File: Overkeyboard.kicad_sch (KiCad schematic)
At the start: 329 parts, among them SW1 SW_Push, SW10 SW_Push, SW100 SW_Push, SW101 SW_Push, SW102 SW_Push, SW103 SW_Push, SW104 SW_Push, SW105 SW_Push, SW106 SW_Push, SW107 SW_Push, SW108 SW_Push, SW109 SW_Push, SW11 SW_Push, SW110 SW_Push, SW111 SW_Push, SW112 SW_Push, SW113 SW_Push, SW114 SW_Push, SW115 SW_Push, SW116 SW_Push, SW117 SW_Push, SW118 SW_Push, SW119 SW_Push, SW12 SW_Push, SW120 SW_Push, SW121 SW_Push, SW122 SW_Push, SW123 SW_Push, SW124 SW_Push, SW125 SW_Push, SW126 SW_Push, SW127 SW_Push, SW128 SW_Push, SW129 SW_Push, SW13 SW_Push, SW130 SW_Push, SW131 SW_Push, SW132 SW_Push, SW133 SW_Push, SW134 SW_Push, SW135 SW_Push, SW136 SW_Push, SW137 SW_Push, SW138 SW_Push, SW139 SW_Push, SW14 SW_Push, SW140 SW_Push, SW141 SW_Push, SW142 SW_Push, SW143 SW_Push, SW144 SW_Push, SW145 SW_Push, SW146 SW_Push, SW147 SW_Push, SW148 SW_Push, SW149 SW_Push, SW15 SW_Push, SW150 SW_Push, SW151 SW_Push, SW152 SW_Push, SW153 SW_Push, SW154 SW_Push, SW155 SW_Push, SW156 SW_Push, SW157 SW_Push, SW16 SW_Push, SW17 SW_Push, SW18 SW_Push, SW19 SW_Push, SW2 SW_Push, SW20 SW_Push, SW21 SW_Push, SW22 SW_Push, SW23 SW_Push, SW24 SW_Push, SW25 SW_Push, SW26 SW_Push, SW27 SW_Push, SW28 SW_Push, SW29 SW_Push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

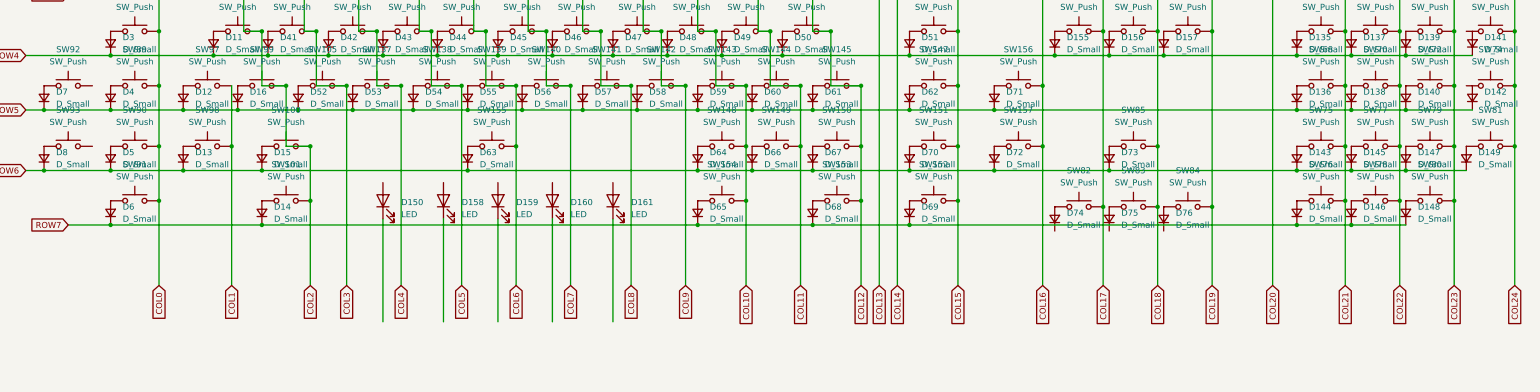
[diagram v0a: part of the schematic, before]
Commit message: added footprints
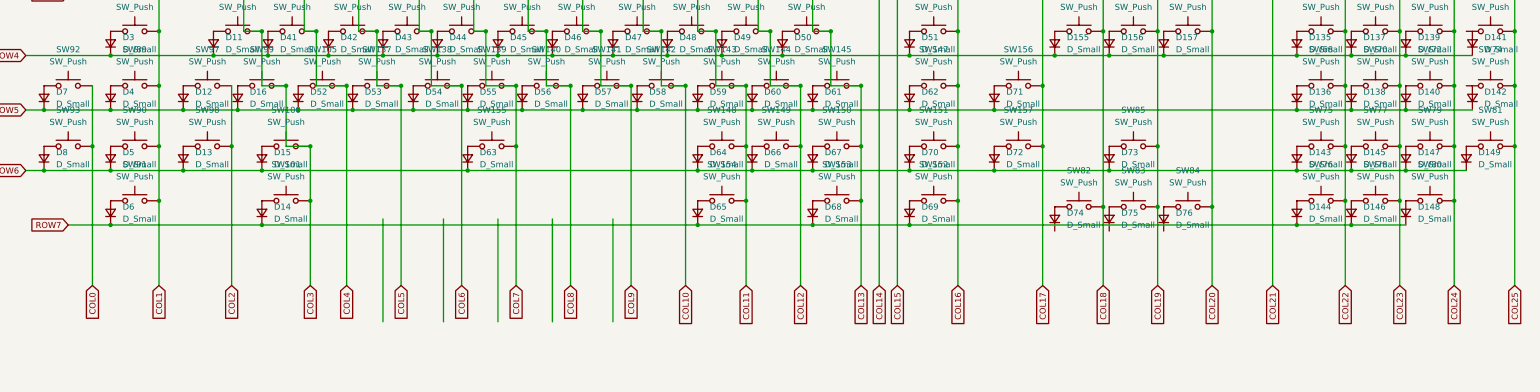
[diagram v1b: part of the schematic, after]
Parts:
- removed D150, D158, D159, D160, D161: LED, symbol Device:LED
- C1, C2, C3: footprint (none) -> Capacitor_SMD:C_0805_2012Metric_Pad1.18x1.45mm_HandSolder
- D1, D10, D100, D101, D102, D103, D104, D105, D106, D107, D108, D109, D11, D110, D111, D112, D113, D114, D115, D116, D117, D118, D119, D12, D120, D121, D122, D123, D124, D125, D126, D127, D128, D129, D13, D130, D131, D132, D133, D134, D135, D136, D137, D138, D139, D14, D140, D141, D142, D143, D144, D145, D146, D147, D148, D149, D15, D151, D152, D153, D154, D155, D156, D157, D16, D17, D18, D19, D2, D20, D21, D22, D23, D24, D25, D26, D27, D28, D29, D3, D30, D31, D32, D33, D34, D35, D36, D37, D38, D39, D4, D40, D41, D42, D43, D44, D45, D46, D47, D48, D49, D5, D50, D51, D52, D53, D54, D55, D56, D57, D58, D59, D6, D60, D61, D62, D63, D64, D65, D66, D67, D68, D69, D7, D70, D71, D72, D73, D74, D75, D76, D77, D78, D79, D8, D80, D81, D82, D83, D84, D85, D86, D87, D88, D89, D9, D90, D91, D92, D93, D94, D95, D96, D97, D98, D99: footprint (none) -> Diode_SMD:D_SOD-123
- F1: footprint (none) -> Fuse:Fuse_1206_3216Metric_Pad1.42x1.75mm_HandSolder
- R1, R2, R3, R4: footprint (none) -> Resistor_SMD:R_0805_2012Metric_Pad1.20x1.40mm_HandSolder
- SW1: footprint (none) -> random-keyboard-parts:SKQG-1155865
- SW10, SW100, SW101, SW102, SW103, SW104, SW105, SW106, SW107, SW108, SW109, SW11, SW110, SW111, SW112, SW113, SW114, SW115, SW116, SW117, SW118, SW119, SW12, SW120, SW121, SW122, SW123, SW124, SW125, SW126, SW127, SW128, SW129, SW13, SW130, SW131, SW132, SW133, SW134, SW135, SW136, SW137, SW138, SW139, SW14, SW140, SW141, SW142, SW143, SW144, SW145, SW146, SW147, SW148, SW149, SW15, SW150, SW151, SW152, SW153, SW154, SW155, SW156, SW157, SW16, SW17, SW18, SW19, SW2, SW20, SW21, SW22, SW23, SW24, SW25, SW26, SW27, SW28, SW29, SW3, SW30, SW31, SW32, SW33, SW34, SW35, SW36, SW37, SW38, SW39, SW4, SW40, SW41, SW42, SW43, SW44, SW45, SW46, SW47, SW48, SW49, SW5, SW50, SW51, SW52, SW53, SW54, SW55, SW56, SW57, SW58, SW59, SW6, SW60, SW61, SW62, SW63, SW64, SW65, SW66, SW67, SW68, SW69, SW7, SW70, SW71, SW72, SW73, SW74, SW75, SW76, SW77, SW78, SW79, SW8, SW80, SW81, SW82, SW83, SW84, SW85, SW86, SW87, SW88, SW89, SW9, SW90, SW91, SW92, SW93, SW94, SW95, SW96, SW97, SW98, SW99: footprint (none) -> MX_Alps_Hybrid:MX-Alps-Hybrid-1U
- USB1: footprint (none) -> random-keyboard-parts:Molex-0548190589
- Y1: footprint (none) -> Crystal:Crystal_SMD_3225-4Pin_3.2x2.5mm_HandSoldering
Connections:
- net COL0: now also SW92.2, SW93.2; no longer SW2.2, SW3.2, SW86.2, SW87.2, SW88.2, SW89.2, SW90.2, SW91.2
- net COL1: now also SW2.2, SW3.2, SW86.2, SW87.2, SW88.2, SW89.2, SW90.2, SW91.2; no longer SW97.2, SW98.2
- net COL10: now also SW111.2, SW123.2, SW133.2, SW142.2, SW16.2, SW17.2; no longer SW112.2, SW124.2, SW134.2, SW143.2, SW148.2, SW154.2, SW18.2, SW19.2
- net COL11: now also SW112.2, SW124.2, SW134.2, SW143.2, SW148.2, SW154.2, SW18.2, SW19.2; no longer SW113.2, SW125.2, SW135.2, SW144.2, SW149.2
- net COL12: now also SW113.2, SW125.2, SW135.2, SW144.2, SW149.2; no longer SW114.2, SW126.2, SW136.2, SW145.2, SW150.2, SW153.2, SW20.2, SW21.2
- net COL13: now also SW114.2, SW126.2, SW136.2, SW145.2, SW150.2, SW153.2, SW20.2, SW21.2; no longer SW115.2, SW127.2, SW22.2, SW23.2
- net COL14: now also SW115.2, SW127.2, SW22.2, SW23.2; no longer SW116.2, SW24.2, SW25.2
- net COL15: now also SW116.2, SW24.2, SW25.2; no longer SW117.2, SW146.2, SW147.2, SW151.2, SW152.2, SW26.2, SW27.2
- net COL16: now also SW117.2, SW146.2, SW147.2, SW151.2, SW152.2, SW26.2, SW27.2; no longer SW156.2, SW157.2, SW28.2, SW29.2, SW46.2, SW47.2
- net COL17: now also SW156.2, SW157.2, SW28.2, SW29.2, SW46.2, SW47.2; no longer SW30.2, SW31.2, SW48.2, SW49.2, SW56.2, SW82.2
- net COL18: now also SW30.2, SW31.2, SW48.2, SW49.2, SW56.2, SW82.2; no longer SW32.2, SW33.2, SW50.2, SW51.2, SW57.2, SW83.2, SW85.2
- net COL19: now also SW32.2, SW33.2, SW50.2, SW51.2, SW57.2, SW83.2, SW85.2; no longer SW34.2, SW35.2, SW52.2, SW53.2, SW58.2, SW84.2
- net COL2: now also SW97.2, SW98.2; no longer SW100.2, SW101.2, SW94.2, SW95.2, SW96.2, SW99.2
- net COL20: now also SW34.2, SW35.2, SW52.2, SW53.2, SW58.2, SW84.2; no longer SW36.2, SW37.2, SW54.2, SW55.2
- net COL21: now also SW36.2, SW37.2, SW54.2, SW55.2; no longer SW38.2, SW39.2, SW59.2, SW60.2, SW67.2, SW68.2, SW75.2, SW76.2
- net COL22: now also SW38.2, SW39.2, SW59.2, SW60.2, SW67.2, SW68.2, SW75.2, SW76.2; no longer SW40.2, SW41.2, SW61.2, SW62.2, SW69.2, SW70.2, SW77.2, SW78.2
- net COL23: now also SW40.2, SW41.2, SW61.2, SW62.2, SW69.2, SW70.2, SW77.2, SW78.2; no longer SW42.2, SW43.2, SW63.2, SW64.2, SW71.2, SW72.2, SW79.2, SW80.2
- net COL24: now also SW42.2, SW43.2, SW63.2, SW64.2, SW71.2, SW72.2, SW79.2, SW80.2; no longer SW44.2, SW45.2, SW65.2, SW66.2, SW73.2, SW74.2, SW81.2
- net COL3: now also SW100.2, SW101.2, SW94.2, SW95.2, SW96.2, SW99.2; no longer SW102.2, SW103.2, SW104.2, SW105.2, SW4.2, SW5.2
- net COL4: now also SW102.2, SW103.2, SW104.2, SW105.2, SW4.2, SW5.2; no longer SW106.2, SW118.2, SW128.2, SW137.2, SW6.2, SW7.2
- net COL5: now also SW106.2, SW118.2, SW128.2, SW137.2, SW6.2, SW7.2; no longer SW107.2, SW119.2, SW129.2, SW138.2, SW8.2, SW9.2
- net COL6: now also SW107.2, SW119.2, SW129.2, SW138.2, SW8.2, SW9.2; no longer SW10.2, SW108.2, SW11.2, SW120.2, SW130.2, SW139.2, SW155.2
- net COL7: now also SW10.2, SW108.2, SW11.2, SW120.2, SW130.2, SW139.2, SW155.2; no longer SW109.2, SW12.2, SW121.2, SW13.2, SW131.2, SW140.2
- net COL8: now also SW109.2, SW12.2, SW121.2, SW13.2, SW131.2, SW140.2; no longer SW110.2, SW122.2, SW132.2, SW14.2, SW141.2, SW15.2
- net COL9: now also SW110.2, SW122.2, SW132.2, SW14.2, SW141.2, SW15.2; no longer SW111.2, SW123.2, SW133.2, SW142.2, SW16.2, SW17.2
- new net COL25: SW44.2, SW45.2, SW65.2, SW66.2, SW73.2, SW74.2, SW81.2

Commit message: It should be fully wired now
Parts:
- added C4, C5, C6: 0.1μF, Capacitor_SMD:C_0805_2012Metric_Pad1.18x1.45mm_HandSolder, symbol Device:C_Small
- added C7: 10μF, Capacitor_SMD:C_0805_2012Metric_Pad1.18x1.45mm_HandSolder, symbol Device:C_Small
- SW100, SW148, SW149, SW150, SW151, SW154, SW156, SW157, SW89, SW90, SW92, SW93, SW98: footprint MX_Alps_Hybrid:MX-Alps-Hybrid-1U -> MX_Alps_Hybrid:MX-Alps-Hybrid-1.25U
- SW101, SW147, SW152, SW88: footprint MX_Alps_Hybrid:MX-Alps-Hybrid-1U -> MX_Alps_Hybrid:MX-Alps-Hybrid-1.75U
- SW146: footprint MX_Alps_Hybrid:MX-Alps-Hybrid-1U -> MX_Alps_Hybrid:MX-Alps-Hybrid-ISO
- SW153, SW91: footprint MX_Alps_Hybrid:MX-Alps-Hybrid-1U -> MX_Alps_Hybrid:MX-Alps-Hybrid-2U
- SW155: footprint MX_Alps_Hybrid:MX-Alps-Hybrid-1U -> MX_Alps_Hybrid:MX-Alps-Hybrid-6.25U
- SW81: footprint MX_Alps_Hybrid:MX-Alps-Hybrid-1U -> MX_Alps_Hybrid:MX-Alps-Hybrid-2U-Vertical
- SW87: footprint MX_Alps_Hybrid:MX-Alps-Hybrid-1U -> MX_Alps_Hybrid:MX-Alps-Hybrid-1.5U
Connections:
- net +5V: now also C4.1, C5.1, C6.1, C7.1
- net COL0: now also SW92.1, SW93.1, U1.33 (PE0); no longer SW92.2, SW93.2
- net COL1: now also SW2.1, SW3.1, SW86.1, SW87.1, SW88.1, SW89.1, SW90.1, SW91.1, U1.34 (PE1); no longer SW2.2, SW3.2, SW86.2, SW87.2, SW88.2, SW89.2, SW90.2, SW91.2
- net COL10: now also SW111.1, SW123.1, SW133.1, SW142.1, SW16.1, SW17.1, U1.44 (PA7); no longer SW111.2, SW123.2, SW133.2, SW142.2, SW16.2, SW17.2
- net COL11: now also SW112.1, SW124.1, SW134.1, SW143.1, SW148.1, SW154.1, SW18.1, SW19.1, U1.45 (PA6); no longer SW112.2, SW124.2, SW134.2, SW143.2, SW148.2, SW154.2, SW18.2, SW19.2
- net COL12: now also SW113.1, SW125.1, SW135.1, SW144.1, SW149.1, SW153.1, U1.46 (PA5); no longer SW113.2, SW125.2, SW135.2, SW144.2, SW149.2
- net COL13: now also SW114.1, SW126.1, SW136.1, SW145.1, SW150.1, SW20.1, SW21.1, U1.47 (PA4); no longer SW114.2, SW126.2, SW136.2, SW145.2, SW150.2, SW153.2, SW20.2, SW21.2
- net COL14: now also SW115.1, SW127.1, SW22.1, SW23.1, U1.48 (PA3); no longer SW115.2, SW127.2, SW22.2, SW23.2
- net COL15: now also SW116.1, SW24.1, SW25.1, U1.49 (PA2); no longer SW116.2, SW24.2, SW25.2
- net COL16: now also SW117.1, SW146.1, SW147.1, SW151.1, SW152.1, SW26.1, SW27.1, U1.50 (PA1); no longer SW117.2, SW146.2, SW147.2, SW151.2, SW152.2, SW26.2, SW27.2
- net COL17: now also SW156.1, SW157.1, SW28.1, SW29.1, SW46.1, SW47.1, U1.51 (PA0); no longer SW156.2, SW157.2, SW28.2, SW29.2, SW46.2, SW47.2
- net COL18: now also SW30.1, SW31.1, SW48.1, SW49.1, SW56.1, SW82.1, U1.61 (PF0); no longer SW30.2, SW31.2, SW48.2, SW49.2, SW56.2, SW82.2
- net COL19: now also SW32.1, SW33.1, SW50.1, SW51.1, SW57.1, SW83.1, SW85.1, U1.60 (PF1); no longer SW32.2, SW33.2, SW50.2, SW51.2, SW57.2, SW83.2, SW85.2
- net COL2: now also SW97.1, SW98.1, U1.35 (PC0); no longer SW97.2, SW98.2
- net COL20: now also SW34.1, SW35.1, SW52.1, SW53.1, SW58.1, SW84.1, U1.59 (PF2); no longer SW34.2, SW35.2, SW52.2, SW53.2, SW58.2, SW84.2
- net COL21: now also SW36.1, SW37.1, SW54.1, SW55.1, U1.58 (PF3); no longer SW36.2, SW37.2, SW54.2, SW55.2
- net COL22: now also SW38.1, SW39.1, SW59.1, SW60.1, SW67.1, SW68.1, SW75.1, SW76.1, U1.57 (PF4); no longer SW38.2, SW39.2, SW59.2, SW60.2, SW67.2, SW68.2, SW75.2, SW76.2
- net COL23: now also SW40.1, SW41.1, SW61.1, SW62.1, SW69.1, SW70.1, SW77.1, SW78.1, U1.56 (PF5); no longer SW40.2, SW41.2, SW61.2, SW62.2, SW69.2, SW70.2, SW77.2, SW78.2
- net COL24: now also SW42.1, SW43.1, SW63.1, SW64.1, SW71.1, SW72.1, SW79.1, SW80.1, U1.55 (PF6); no longer SW42.2, SW43.2, SW63.2, SW64.2, SW71.2, SW72.2, SW79.2, SW80.2
- net COL25: now also SW44.1, SW45.1, SW65.1, SW66.1, SW73.1, SW74.1, SW81.1, U1.54 (PF7); no longer SW44.2, SW45.2, SW65.2, SW66.2, SW73.2, SW74.2, SW81.2
- net COL3: now also SW100.1, SW101.1, SW94.1, SW95.1, SW96.1, SW99.1, U1.36 (PC1); no longer SW100.2, SW101.2, SW94.2, SW95.2, SW96.2, SW99.2
- net COL4: now also SW102.1, SW103.1, SW104.1, SW105.1, SW4.1, SW5.1, U1.37 (PC2); no longer SW102.2, SW103.2, SW104.2, SW105.2, SW4.2, SW5.2
- net COL5: now also SW106.1, SW118.1, SW128.1, SW137.1, SW6.1, SW7.1, U1.38 (PC3); no longer SW106.2, SW118.2, SW128.2, SW137.2, SW6.2, SW7.2
- net COL6: now also SW107.1, SW119.1, SW129.1, SW138.1, SW8.1, SW9.1, U1.39 (PC4); no longer SW107.2, SW119.2, SW129.2, SW138.2, SW8.2, SW9.2
- net COL7: now also SW10.1, SW108.1, SW11.1, SW120.1, SW130.1, SW139.1, SW155.1, U1.40 (PC5); no longer SW10.2, SW108.2, SW11.2, SW120.2, SW130.2, SW139.2, SW155.2
- net COL8: now also SW109.1, SW12.1, SW121.1, SW13.1, SW131.1, SW140.1, U1.41 (PC6); no longer SW109.2, SW12.2, SW121.2, SW13.2, SW131.2, SW140.2
- net COL9: now also SW110.1, SW122.1, SW132.1, SW14.1, SW141.1, SW15.1, U1.42 (PC7); no longer SW110.2, SW122.2, SW132.2, SW14.2, SW141.2, SW15.2
- net GND: now also C4.2, C5.2, C6.2, C7.2
- net ROW0: now also D101.1 (K), D103.1 (K), D105.1 (K), D107.1 (K), D109.1 (K), D119.1 (K), D121.1 (K), D123.1 (K), D125.1 (K), D151.1 (K), U1.9 (PE3)
- net ROW1: now also U1.10 (PB0)
- net ROW2: now also U1.11 (PB1)
- net ROW3: now also U1.12 (PB2)
- net ROW4: now also D7.1 (K), U1.13 (PB3)
- net ROW5: now also D8.1 (K), U1.14 (PB4); no longer D7.1 (K)
- net ROW6: now also U1.15 (PB5); no longer D8.1 (K)
- net ROW7: now also D74.1 (K), D75.1 (K), D76.1 (K), U1.16 (PB6)
- net VCC: now also USB1.5 (VBUS); no longer USB1.6 (SHIELD)
- net at D20.2 (A): now also SW107.2; no longer SW107.1
- net at D21.2 (A): now also SW108.2; no longer SW108.1
- net at D62.2 (A): now also SW147.2; no longer SW147.1
- net at D13.2 (A): now also SW98.2; no longer SW98.1
- net at D103.2 (A): now also SW28.2; no longer SW28.1
- net at D30.2 (A): now also SW117.2; no longer SW117.1
- net at D54.2 (A): now also SW138.2; no longer SW138.1
- net at D64.2 (A): now also SW148.2; no longer SW148.1
- net at D122.2 (A): now also SW41.2; no longer SW41.1
- net at D126.2 (A): now also SW45.2; no longer SW45.1
- net at D87.2 (A): now also SW12.2; no longer SW12.1
- net at D73.2 (A): now also SW85.2; no longer SW85.1
- net at D46.2 (A): now also SW132.2; no longer SW132.1
- net at D67.2 (A): now also SW150.2; no longer SW150.1
- net at D34.2 (A): now also SW121.2; no longer SW121.1
- net at D138.2 (A): now also SW70.2; no longer SW70.1
- net at D4.2 (A): now also SW89.2; no longer SW89.1
- net at D127.2 (A): now also SW59.2; no longer SW59.1
- net at D109.2 (A): now also SW34.2; no longer SW34.1
- net at D55.2 (A): now also SW139.2; no longer SW139.1
- net at D56.2 (A): now also SW140.2; no longer SW140.1
- net at D69.2 (A): now also SW152.2; no longer SW152.1
- net at D82.2 (A): now also SW7.2; no longer SW7.1
- net at D71.2 (A): now also SW156.2; no longer SW156.1
- net at D90.2 (A): now also SW15.2; no longer SW15.1
- net at D9.2 (A): now also SW94.2; no longer SW94.1
- net at D144.2 (A): now also SW76.2; no longer SW76.1
- net at D93.2 (A): now also SW18.2; no longer SW18.1
- net at D99.2 (A): now also SW24.2; no longer SW24.1
- net at D39.2 (A): now also SW126.2; no longer SW126.1
- net at D57.2 (A): now also SW141.2; no longer SW141.1
- net at D74.2 (A): now also SW82.2; no longer SW82.1
- net at D111.2 (A): now also SW46.2; no longer SW46.1
- net at D104.2 (A): now also SW29.2; no longer SW29.1
- net at D92.2 (A): now also SW17.2; no longer SW17.1
- net at D115.2 (A): now also SW50.2; no longer SW50.1
- net at D36.2 (A): now also SW123.2; no longer SW123.1
- net at D116.2 (A): now also SW51.2; no longer SW51.1
- net at D155.2 (A): now also SW56.2; no longer SW56.1
- net at D77.2 (A): now also SW2.2; no longer SW2.1
- net at D6.2 (A): now also SW91.2; no longer SW91.1
- net at D25.2 (A): now also SW112.2; no longer SW112.1
- net at D66.2 (A): now also SW149.2; no longer SW149.1
- net at D81.2 (A): now also SW6.2; no longer SW6.1
- net at D41.2 (A): now also SW104.2; no longer SW104.1
- net at D49.2 (A): now also SW135.2; no longer SW135.1
- net at D11.2 (A): now also SW96.2; no longer SW96.1
- net at D105.2 (A): now also SW30.2; no longer SW30.1
- net at D154.2 (A): now also SW55.2; no longer SW55.1
- net at D78.2 (A): now also SW3.2; no longer SW3.1
- net at D38.2 (A): now also SW125.2; no longer SW125.1
- net at D7.2 (A): now also SW92.2; no longer SW92.1
- net at D44.2 (A): now also SW130.2; no longer SW130.1
- net at D80.2 (A): now also SW5.2; no longer SW5.1
- net at D60.2 (A): now also SW144.2; no longer SW144.1
- net at D16.2 (A): now also SW99.2; no longer SW99.1
- net at D113.2 (A): now also SW48.2; no longer SW48.1
- net at D86.2 (A): now also SW11.2; no longer SW11.1
- net at D72.2 (A): now also SW157.2; no longer SW157.1
- net at D70.2 (A): now also SW151.2; no longer SW151.1
- net at D59.2 (A): now also SW143.2; no longer SW143.1
- net at D121.2 (A): now also SW40.2; no longer SW40.1
- net at D143.2 (A): now also SW75.2; no longer SW75.1
- net at D18.2 (A): now also SW102.2; no longer SW102.1
- net at D53.2 (A): now also SW137.2; no longer SW137.1
- net at D136.2 (A): now also SW68.2; no longer SW68.1
- net at D156.2 (A): now also SW57.2; no longer SW57.1
- net at D32.2 (A): now also SW119.2; no longer SW119.1
- net at D139.2 (A): now also SW71.2; no longer SW71.1
- net at D108.2 (A): now also SW33.2; no longer SW33.1
- net at D97.2 (A): now also SW22.2; no longer SW22.1
- net at D50.2 (A): now also SW136.2; no longer SW136.1
- net at D131.2 (A): now also SW63.2; no longer SW63.1
- net at D112.2 (A): now also SW47.2; no longer SW47.1
- net at D100.2 (A): now also SW25.2; no longer SW25.1
- net at D137.2 (A): now also SW69.2; no longer SW69.1
- net at D8.2 (A): now also SW93.2; no longer SW93.1
- net at D124.2 (A): now also SW43.2; no longer SW43.1
- net at D24.2 (A): now also SW111.2; no longer SW111.1
- net at D88.2 (A): now also SW13.2; no longer SW13.1
- net at D35.2 (A): now also SW122.2; no longer SW122.1
- net at D91.2 (A): now also SW16.2; no longer SW16.1
- net at D123.2 (A): now also SW42.2; no longer SW42.1
- net at D26.2 (A): now also SW113.2; no longer SW113.1
- net at D101.2 (A): now also SW26.2; no longer SW26.1
- net at D157.2 (A): now also SW58.2; no longer SW58.1
- net at D128.2 (A): now also SW60.2; no longer SW60.1
- net at D14.2 (A): now also SW101.2; no longer SW101.1
- net at D27.2 (A): now also SW114.2; no longer SW114.1
- net at D42.2 (A): now also SW128.2; no longer SW128.1
- net at D47.2 (A): now also SW133.2; no longer SW133.1
- net at D117.2 (A): now also SW52.2; no longer SW52.1
- net at D119.2 (A): now also SW38.2; no longer SW38.1
- net at D107.2 (A): now also SW32.2; no longer SW32.1
- net at D130.2 (A): now also SW62.2; no longer SW62.1
- net at D140.2 (A): now also SW72.2; no longer SW72.1
- net at D114.2 (A): now also SW49.2; no longer SW49.1
- net at D145.2 (A): now also SW77.2; no longer SW77.1
- net at D134.2 (A): now also SW66.2
- net at D43.2 (A): now also SW129.2; no longer SW129.1
- net at D125.2 (A): now also SW44.2; no longer SW44.1
- net at D147.2 (A): now also SW79.2; no longer SW79.1
- net at D75.2 (A): now also SW83.2; no longer SW83.1
- net at D85.2 (A): now also SW10.2; no longer SW10.1
- net at D120.2 (A): now also SW39.2; no longer SW39.1
- net at D89.2 (A): now also SW14.2; no longer SW14.1
- net at D135.2 (A): now also SW67.2; no longer SW67.1
- net at D12.2 (A): now also SW97.2; no longer SW97.1
- net at D40.2 (A): now also SW127.2; no longer SW127.1
- net at D68.2 (A): now also SW153.2; no longer SW153.1
- net at D15.2 (A): now also SW100.2; no longer SW100.1
- net at D148.2 (A): now also SW80.2; no longer SW80.1
- net at D83.2 (A): now also SW8.2; no longer SW8.1
- net at D28.2 (A): now also SW115.2; no longer SW115.1
- net at D3.2 (A): now also SW88.2; no longer SW88.1
- net at D37.2 (A): now also SW124.2; no longer SW124.1
- net at D63.2 (A): now also SW155.2; no longer SW155.1
- net at D29.2 (A): now also SW116.2; no longer SW116.1
- net at D102.2 (A): now also SW27.2; no longer SW27.1
- net at D153.2 (A): now also SW54.2; no longer SW54.1
- net at D149.2 (A): now also SW81.2; no longer SW81.1
- net at D2.2 (A): now also SW87.2; no longer SW87.1
- net at D132.2 (A): now also SW64.2; no longer SW64.1
- net at D5.2 (A): now also SW90.2; no longer SW90.1
- net at D61.2 (A): now also SW145.2; no longer SW145.1
- net at D110.2 (A): now also SW35.2; no longer SW35.1
- net at D22.2 (A): now also SW109.2; no longer SW109.1
- net at D79.2 (A): now also SW4.2; no longer SW4.1
- net at D19.2 (A): now also SW106.2; no longer SW106.1
- net at D94.2 (A): now also SW19.2; no longer SW19.1
- net at D152.2 (A): now also SW37.2; no longer SW37.1
- net at D58.2 (A): now also SW142.2; no longer SW142.1
- net at D151.2 (A): now also SW36.2; no longer SW36.1
- net at D1.2 (A): now also SW86.2; no longer SW86.1
- net at D96.2 (A): now also SW21.2; no longer SW21.1
- net at D31.2 (A): now also SW118.2; no longer SW118.1
- net at D10.2 (A): now also SW95.2; no longer SW95.1
- net at D33.2 (A): now also SW120.2; no longer SW120.1
- net at D51.2 (A): now also SW146.2; no longer SW146.1
- net at D106.2 (A): now also SW31.2; no longer SW31.1
- net at D48.2 (A): now also SW134.2; no longer SW134.1
- net at D45.2 (A): now also SW131.2; no longer SW131.1
- net at D17.2 (A): now also SW103.2; no longer SW103.1
- net at D98.2 (A): now also SW23.2; no longer SW23.1
- net at D129.2 (A): now also SW61.2; no longer SW61.1
- net at D23.2 (A): now also SW110.2; no longer SW110.1
- net at D146.2 (A): now also SW78.2; no longer SW78.1
- net at D133.2 (A): now also SW65.2
- net at D118.2 (A): now also SW53.2; no longer SW53.1
- net at D52.2 (A): now also SW105.2; no longer SW105.1
- net at D142.2 (A): now also SW74.2
- net at D95.2 (A): now also SW20.2; no longer SW20.1
- net at D84.2 (A): now also SW9.2; no longer SW9.1
- net at D141.2 (A): now also SW73.2
- net at D65.2 (A): now also SW154.2; no longer SW154.1
- net at D76.2 (A): now also SW84.2; no longer SW84.1
- net +D renamed D+
- net -D renamed D-
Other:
- moved on the sheet: D133, D134, D141, D142, D68, D7, D74, D75, D76, D8, F1, R1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

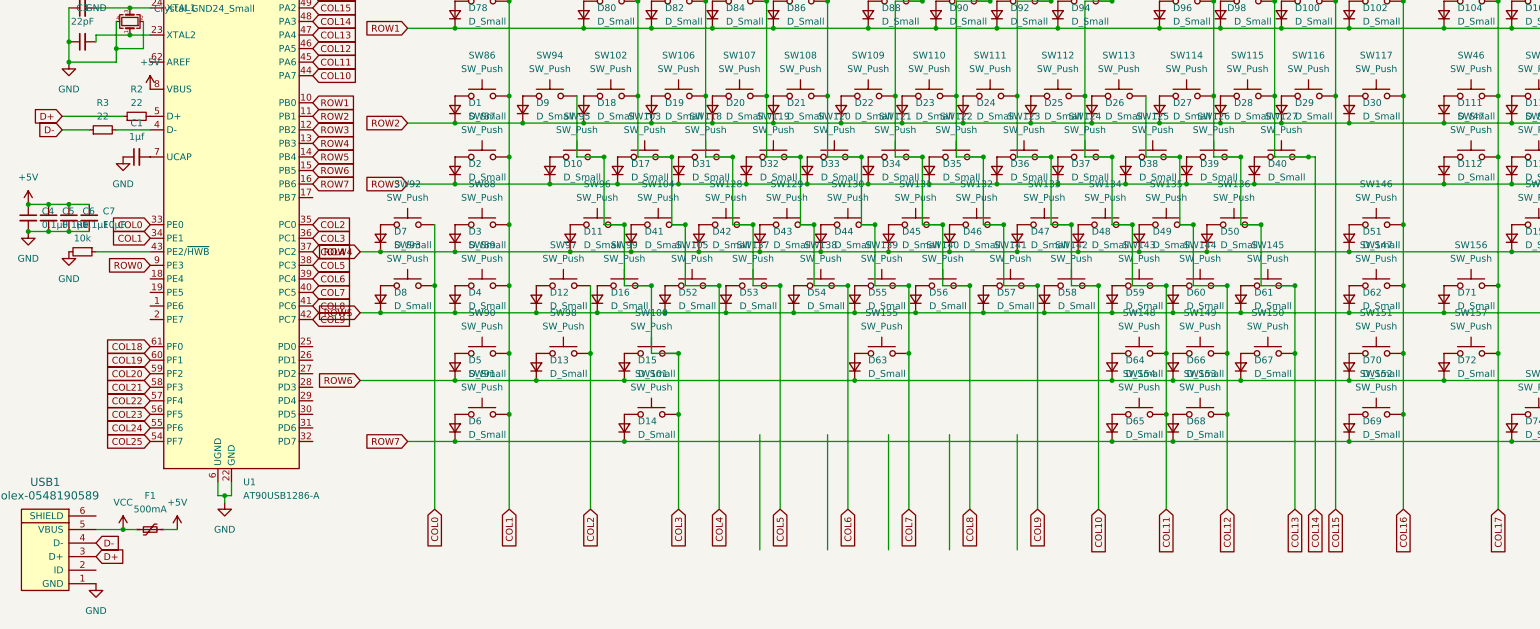
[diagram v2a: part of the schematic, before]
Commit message: Almost fully wired excepting figuring out what LED and resistor values to use
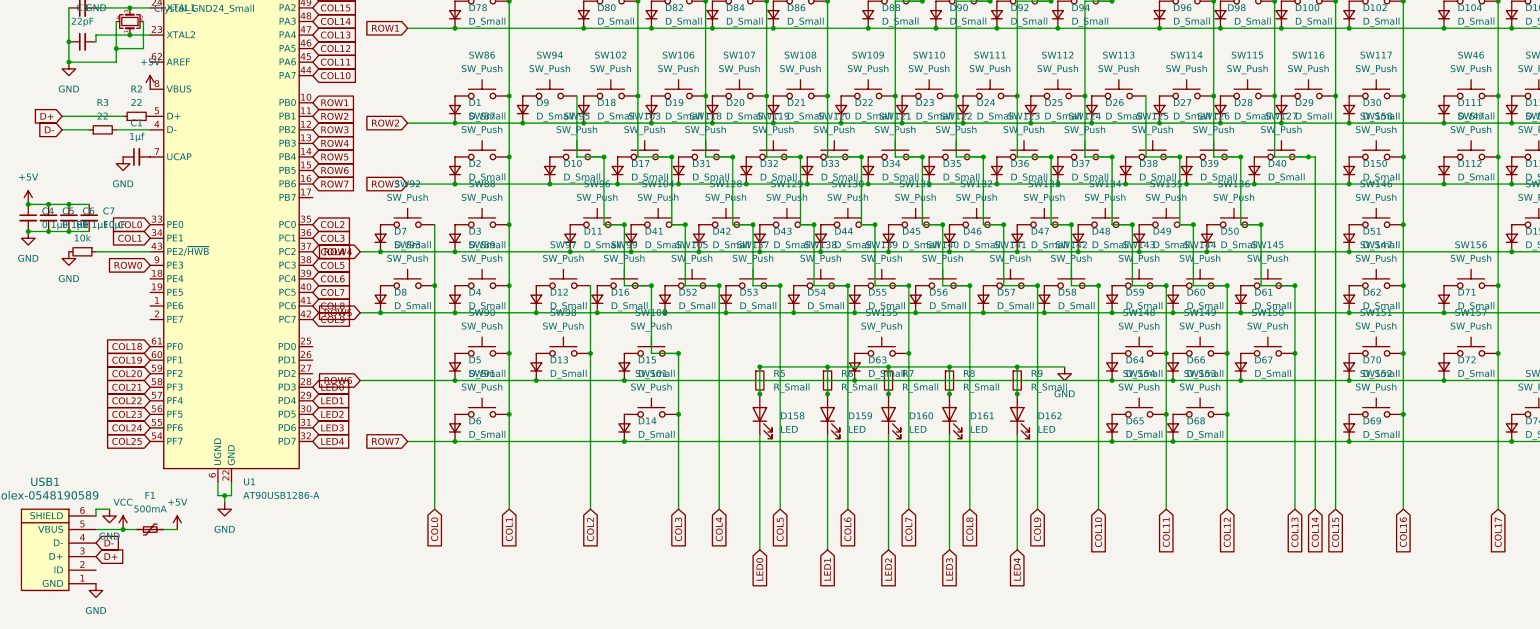
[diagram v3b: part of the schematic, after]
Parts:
- added D150: D_Small, Diode_SMD:D_SOD-123, symbol Device:D_Small
- added D158, D159, D160, D161, D162: LED, LED_THT:LED_D5.0mm, symbol Device:LED
- added R5, R6, R7, R8, R9: R_Small, Resistor_SMD:R_0805_2012Metric_Pad1.20x1.40mm_HandSolder, symbol Device:R_Small
- added SW158: SW_Push, MX_Solderable:MX-Solderable-1.5U, symbol Switch:SW_Push
- SW10, SW102, SW103, SW104, SW105, SW106, SW107, SW108, SW109, SW11, SW110, SW111, SW112, SW113, SW114, SW115, SW116, SW117, SW118, SW119, SW12, SW120, SW121, SW122, SW123, SW124, SW125, SW126, SW127, SW128, SW129, SW13, SW130, SW131, SW132, SW133, SW134, SW135, SW136, SW137, SW138, SW139, SW14, SW140, SW141, SW142, SW143, SW144, SW145, SW15, SW16, SW17, SW18, SW19, SW2, SW20, SW21, SW22, SW23, SW24, SW25, SW26, SW27, SW28, SW29, SW3, SW30, SW31, SW32, SW33, SW34, SW35, SW36, SW37, SW38, SW39, SW4, SW40, SW41, SW42, SW43, SW44, SW45, SW46, SW47, SW48, SW49, SW5, SW50, SW51, SW52, SW53, SW54, SW55, SW56, SW57, SW58, SW59, SW6, SW60, SW61, SW62, SW63, SW64, SW65, SW66, SW67, SW68, SW69, SW7, SW70, SW71, SW72, SW73, SW74, SW75, SW76, SW77, SW78, SW79, SW8, SW80, SW82, SW83, SW84, SW85, SW86, SW9, SW94, SW95, SW96, SW97, SW99: footprint MX_Alps_Hybrid:MX-Alps-Hybrid-1U -> MX_Solderable:MX-Solderable-1U
- SW100, SW148, SW149, SW150, SW151, SW154, SW156, SW157, SW89, SW90, SW92, SW93, SW98: footprint MX_Alps_Hybrid:MX-Alps-Hybrid-1.25U -> MX_Solderable:MX-Solderable-1.25U
- SW101, SW147, SW152, SW88: footprint MX_Alps_Hybrid:MX-Alps-Hybrid-1.75U -> MX_Solderable:MX-Solderable-1.75U
- SW146: footprint MX_Alps_Hybrid:MX-Alps-Hybrid-ISO -> MX_Solderable:MX-Solderable-2.25U
- SW153, SW91: footprint MX_Alps_Hybrid:MX-Alps-Hybrid-2U -> MX_Solderable:MX-Solderable-2U
- SW155: footprint MX_Alps_Hybrid:MX-Alps-Hybrid-6.25U -> MX_Solderable:MX-Solderable-6.25U
- SW81: footprint MX_Alps_Hybrid:MX-Alps-Hybrid-2U-Vertical -> MX_Solderable:MX-Solderable-2U-Vertical
- SW87: footprint MX_Alps_Hybrid:MX-Alps-Hybrid-1.5U -> MX_Solderable:MX-Solderable-1.5U
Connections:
- net COL16: now also SW158.1
- net GND: now also USB1.6 (SHIELD), D158.2 (A), D159.2 (A), D160.2 (A), D161.2 (A), D162.2 (A), R5.1, R5.2, R6.1, R6.2, R7.1, R7.2, R8.1, R8.2, R9.1, R9.2
- net ROW3: now also D150.1 (K)
- net LED0: now reaches U1.28 (PD3)
- net LED0: now also D158.1 (K)
- net LED1: now reaches U1.29 (PD4)
- net LED1: now also D159.1 (K)
- net LED2: now reaches U1.30 (PD5)
- net LED2: now also D160.1 (K)
- net LED3: now reaches U1.31 (PD6)
- net LED3: now also D161.1 (K)
- net LED4: now reaches U1.32 (PD7)
- net LED4: now also D162.1 (K)
- new net: D150.2 (A), SW158.2
